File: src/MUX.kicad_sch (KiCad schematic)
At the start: 24 parts, among them U10 TMUX1208QRSVRQ1, U5 PCF8574RGTR(UMW), U6 PCF8574RGTR(UMW), U7 TMUX1208QRSVRQ1, U8 TMUX1208QRSVRQ1, U9 TMUX1208QRSVRQ1

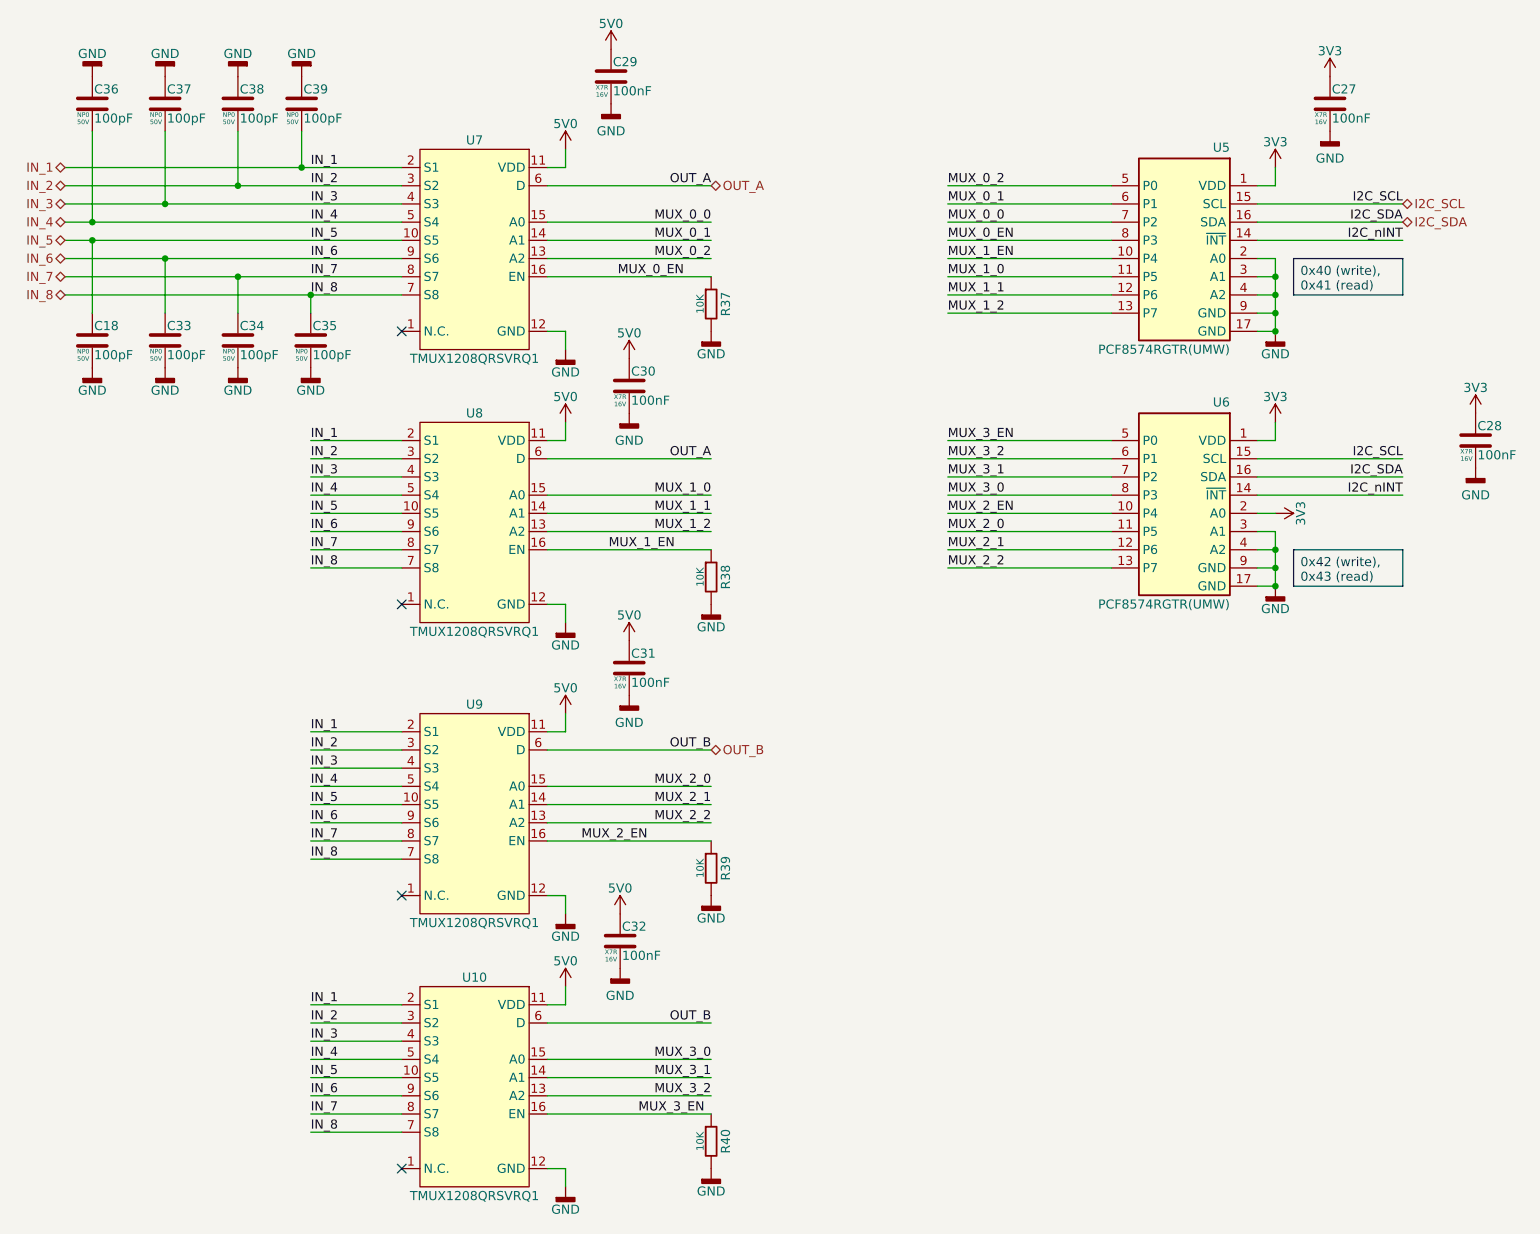
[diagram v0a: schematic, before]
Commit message: V3.1 first changes
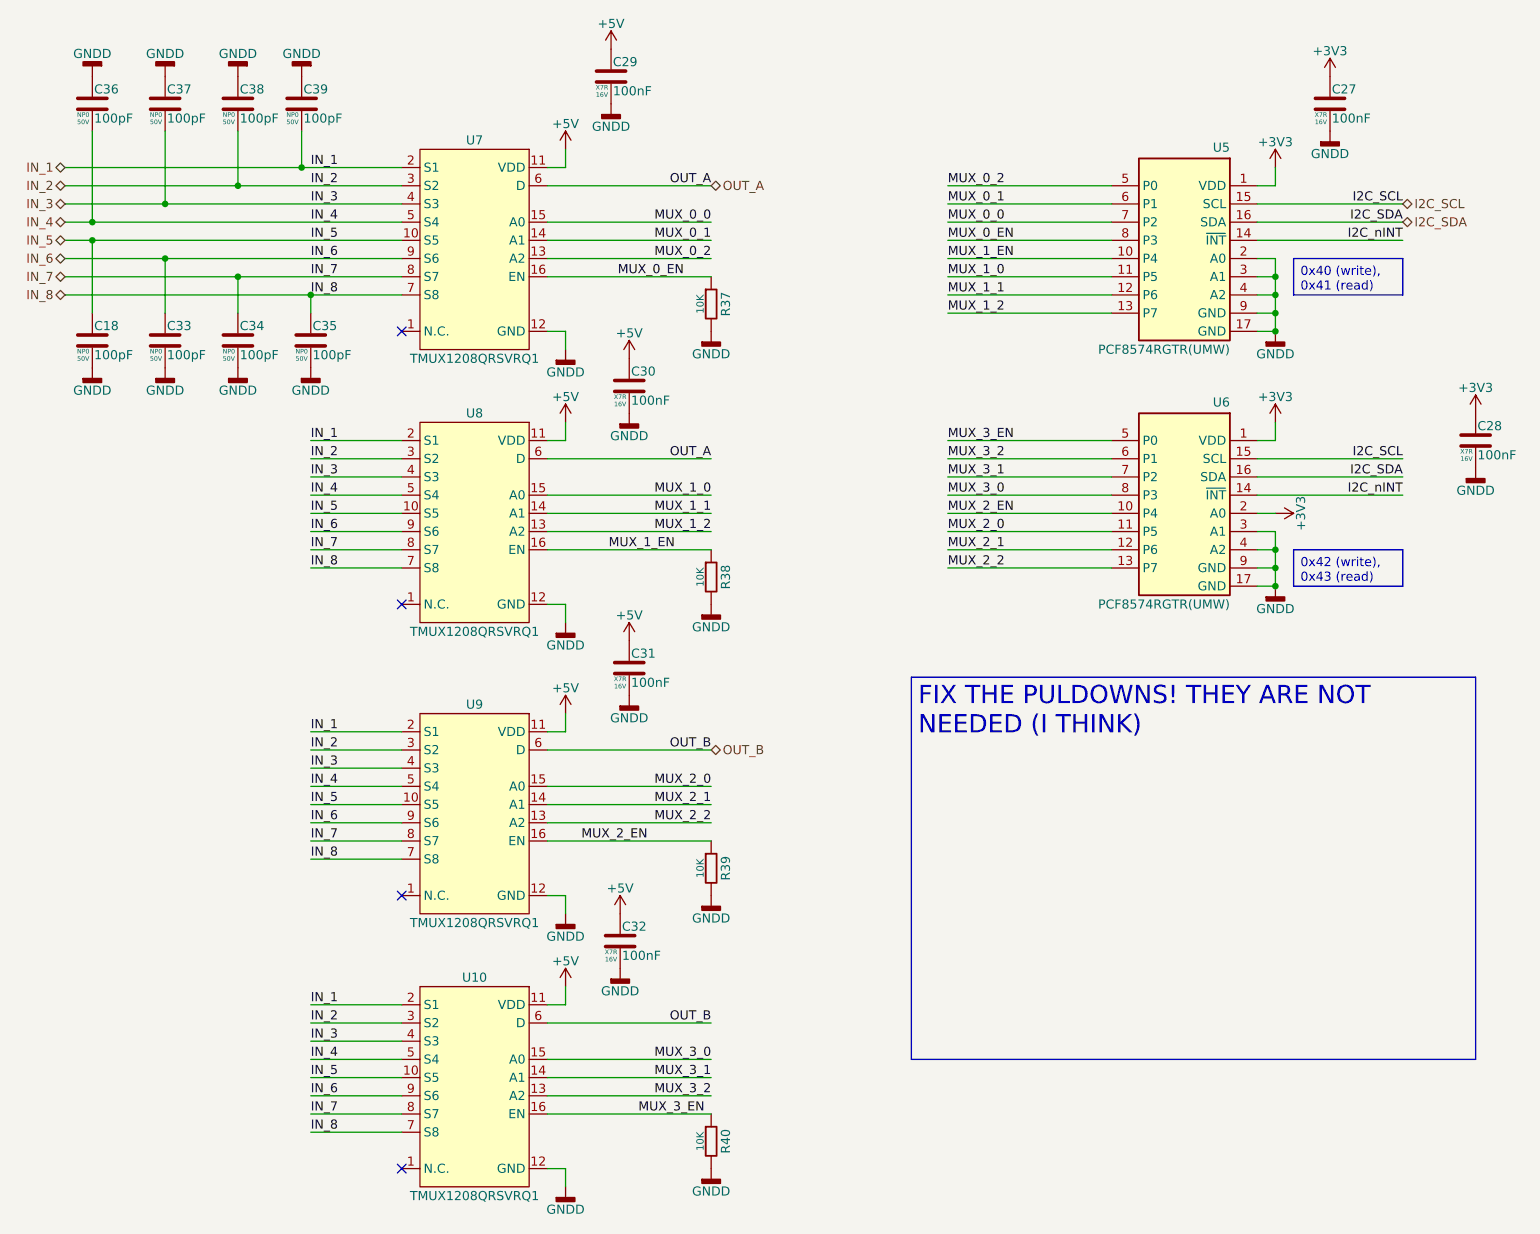
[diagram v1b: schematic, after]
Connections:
- net 3V3 renamed +3V3
- net 5V0 renamed +5V
- net GND renamed GNDD

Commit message: ongoing work
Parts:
- removed R37, R38, R39, R40: 10K, 7Sigma:R_0402_1005Metric, symbol Resistor:0402WGF1002TCE
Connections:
- net +3V3 renamed 3V3
- net +5V renamed 5V0
- net GNDD renamed GND
- net I2C_nINT: no longer names the net of U5.14 (~{INT})
- net I2C_nINT: no longer U6.14 (~{INT})
- no-connect marks 4 -> 6

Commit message: Layout progress
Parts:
- C18, C33, C34, C35, C36, C37, C38, C39: Price @1 USD (none) -> 0.0012; Price @100 USD (none) -> 0.0012; Price @Bulk USD (none) -> 0.0010; Price Bulk Qty (none) -> 1000; Price Source (none) -> LCSC; Price Updated (none) -> 2026-05-14
- C27, C28, C29, C30, C31, C32: Price @1 USD (none) -> 0.0015; Price @100 USD (none) -> 0.0015; Price @Bulk USD (none) -> 0.0012; Price Bulk Qty (none) -> 1000; Price Source (none) -> LCSC; Price Updated (none) -> 2026-05-14
- U10, U7, U8, U9: value TMUX1208QRSVRQ1 -> TMUX1208RSVR; symbol ICs:TMUX1208QRSVRQ1 -> ICs:TMUX1208RSVR; LCSC Part C2876797 -> C2673274; Manufacturer 1 UMW -> Texas Instruments; Manufacturer Part Number 1 TMUX1208QRSVRQ1 -> TMUX1208RSVR; Price @1 USD (none) -> 0.5658; Price @100 USD (none) -> 0.3486; Price @Bulk USD (none) -> 0.2999; Price Bulk Qty (none) -> 1000; Price Source (none) -> LCSC; Price Updated (none) -> 2026-05-14; Supplier Part Number 1 C2876797 -> C2673274
- U5, U6: Price @1 USD (none) -> 0.5030; Price @100 USD (none) -> 0.2854; Price @Bulk USD (none) -> 0.2419; Price Bulk Qty (none) -> 1000; Price Source (none) -> LCSC; Price Updated (none) -> 2026-05-14
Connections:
- net MUX_0_0: now also U5.6 (P1); no longer U5.7 (P2)
- net MUX_0_1: now also U5.7 (P2); no longer U5.6 (P1)
- net MUX_0_2: now also U5.8 (P3); no longer U5.5 (P0)
- net MUX_0_EN: now also U5.5 (P0); no longer U5.8 (P3)
- net MUX_3_0: now also U6.6 (P1); no longer U6.8 (P3)
- net MUX_3_2: now also U6.8 (P3); no longer U6.6 (P1)

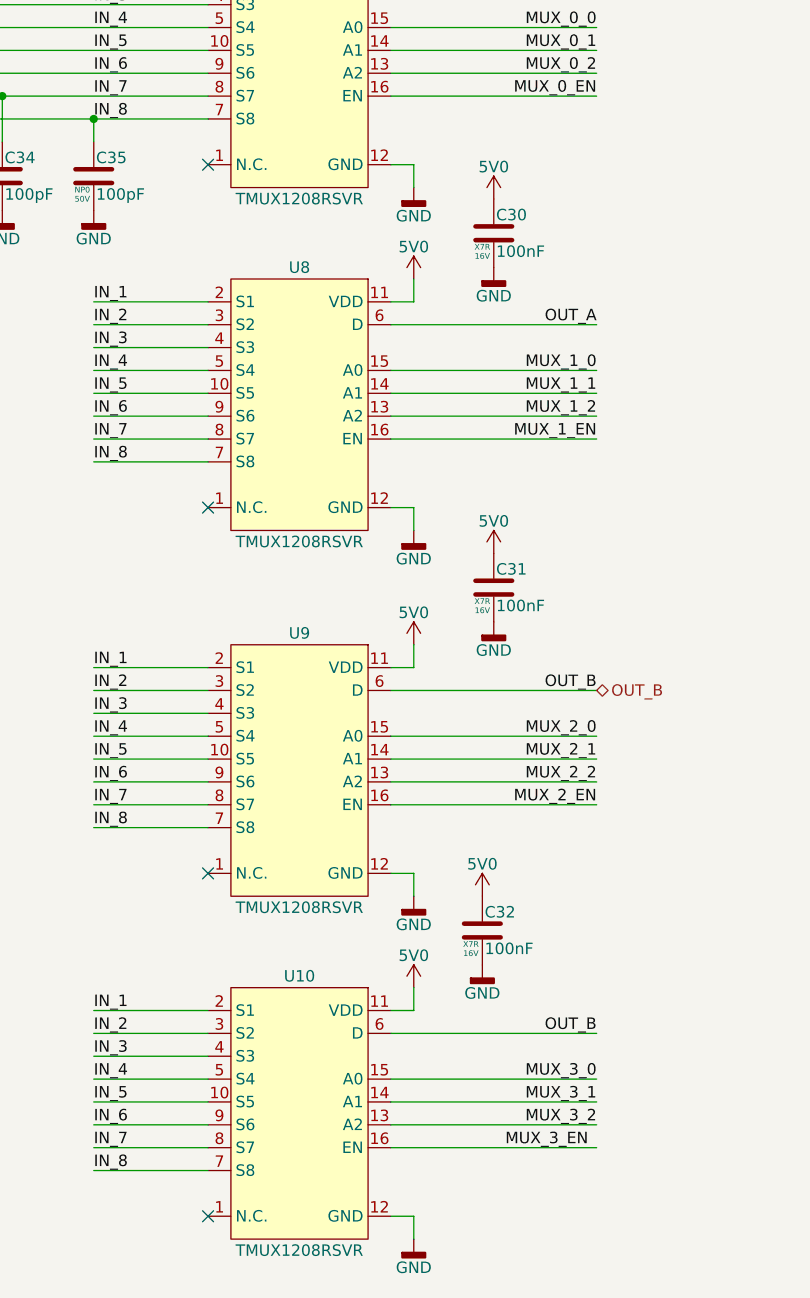
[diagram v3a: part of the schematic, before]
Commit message: schematic cleanup, verification. GPIO9 pin pulldown changed to pullup.
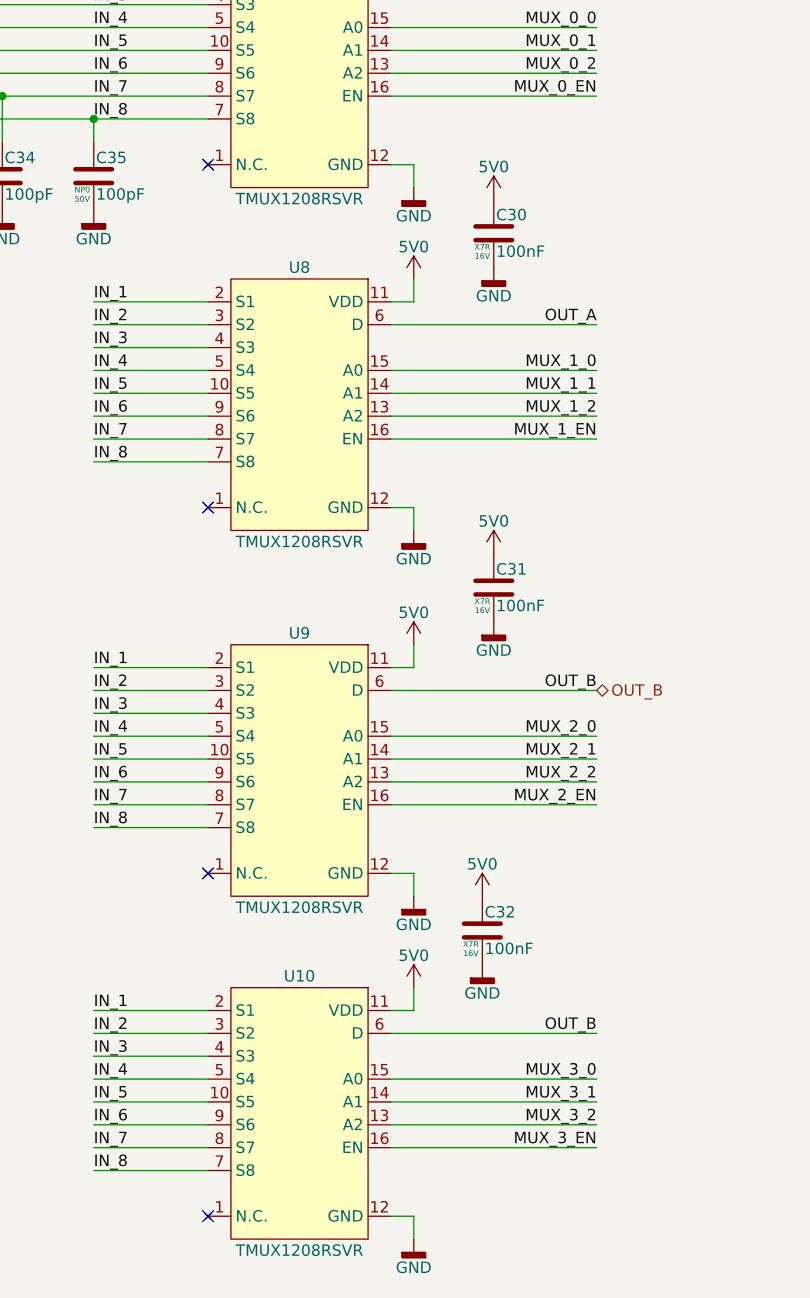
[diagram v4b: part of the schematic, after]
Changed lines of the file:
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@@
 	)
 	(label "MUX_3_EN"
-		(at 104.14 167.64 0)
+		(at 114.3 167.64 180)
 		(effects
 			(font
 				(size 1.27 1.27)
 			)
-			(justify left bottom)
+			(justify right bottom)
 		)
 	)
@@
 			)
 		)
-		(property "Manufacturer" ""
-			(at 81.28 124.46 0)
-			(hide yes)
-			(show_name no)
-			(do_not_autoplace no)
-			(effects
-				(font
-					(size 1.27 1.27)
-				)
-			)
-		)
-		(property "Manufacturer Part Number" ""
-			(at 81.28 124.46 0)
-			(hide yes)
-			(show_name no)
-			(do_not_autoplace no)
-			(effects
-				(font
-					(size 1.27 1.27)
-				)
-			)
-		)
-		(property "on_board" ""
-			(at 81.28 124.46 0)
-			(hide yes)
-			(show_name no)
-			(do_not_autoplace no)
-			(effects
-				(font
-					(size 1.27 1.27)
-				)
-			)
-		)
 		(pin "14"
 		)
@@
 			)
 		)
-		(property "Manufacturer" ""
-			(at 81.28 162.56 0)
-			(hide yes)
-			(show_name no)
-			(do_not_autoplace no)
-			(effects
-				(font
-					(size 1.27 1.27)
-				)
-			)
-		)
-		(property "Manufacturer Part Number" ""
-			(at 81.28 162.56 0)
-			(hide yes)
-			(show_name no)
-			(do_not_autoplace no)
-			(effects
-				(font
-					(size 1.27 1.27)
-				)
-			)
-		)
-		(property "on_board" ""
-			(at 81.28 162.56 0)
-			(hide yes)
-			(show_name no)
-			(do_not_autoplace no)
-			(effects
-				(font
-					(size 1.27 1.27)
-				)
-			)
-		)
 		(pin "14"
 		)
@@
 			)
 		)
-		(property "Manufacturer" ""
-			(at 81.28 83.82 0)
-			(hide yes)
-			(show_name no)
-			(do_not_autoplace no)
-			(effects
-				(font
-					(size 1.27 1.27)
-				)
-			)
-		)
-		(property "Manufacturer Part Number" ""
-			(at 81.28 83.82 0)
-			(hide yes)
-			(show_name no)
-			(do_not_autoplace no)
-			(effects
-				(font
-					(size 1.27 1.27)
-				)
-			)
-		)
-		(property "on_board" ""
-			(at 81.28 83.82 0)
-			(hide yes)
-			(show_name no)
-			(do_not_autoplace no)
-			(effects
-				(font
-					(size 1.27 1.27)
-				)
-			)
-		)
 		(pin "14"
 		)
@@
 				)
 			)
-		)
-		(property "Manufacturer" ""
-			(at 81.28 45.72 0)
-			(hide yes)
-			(show_name no)
-			(do_not_autoplace no)
-			(effects
-				(font
-					(size 1.27 1.27)
-				)
-			)
-		)
-		(property "Manufacturer Part Number" ""
-			(at 81.28 45.72 0)
-			(hide yes)
-			(show_name no)
-			(do_not_autoplace no)
-			(effects
-				(font
-					(size 1.27 1.27)
-				)
-			)
-		)
-		(property "on_board" ""
-			(at 81.28 45.72 0)
-			(hide yes)
-			(show_name no)
-			(do_not_autoplace no)
-			(effects
-				(font
-					(size 1.27 1.27)
-				)
-			)
